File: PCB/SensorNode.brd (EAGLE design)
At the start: 100 x 80 mm, 54 parts, among them Q1 CMA-4544PF-W, U1 MAX4466EXK+T, U2 ESP-WROOM-32, U3 Si7021-A20, U4 MCP73831, U5 TSL2561, U7 V_REG_317SMD

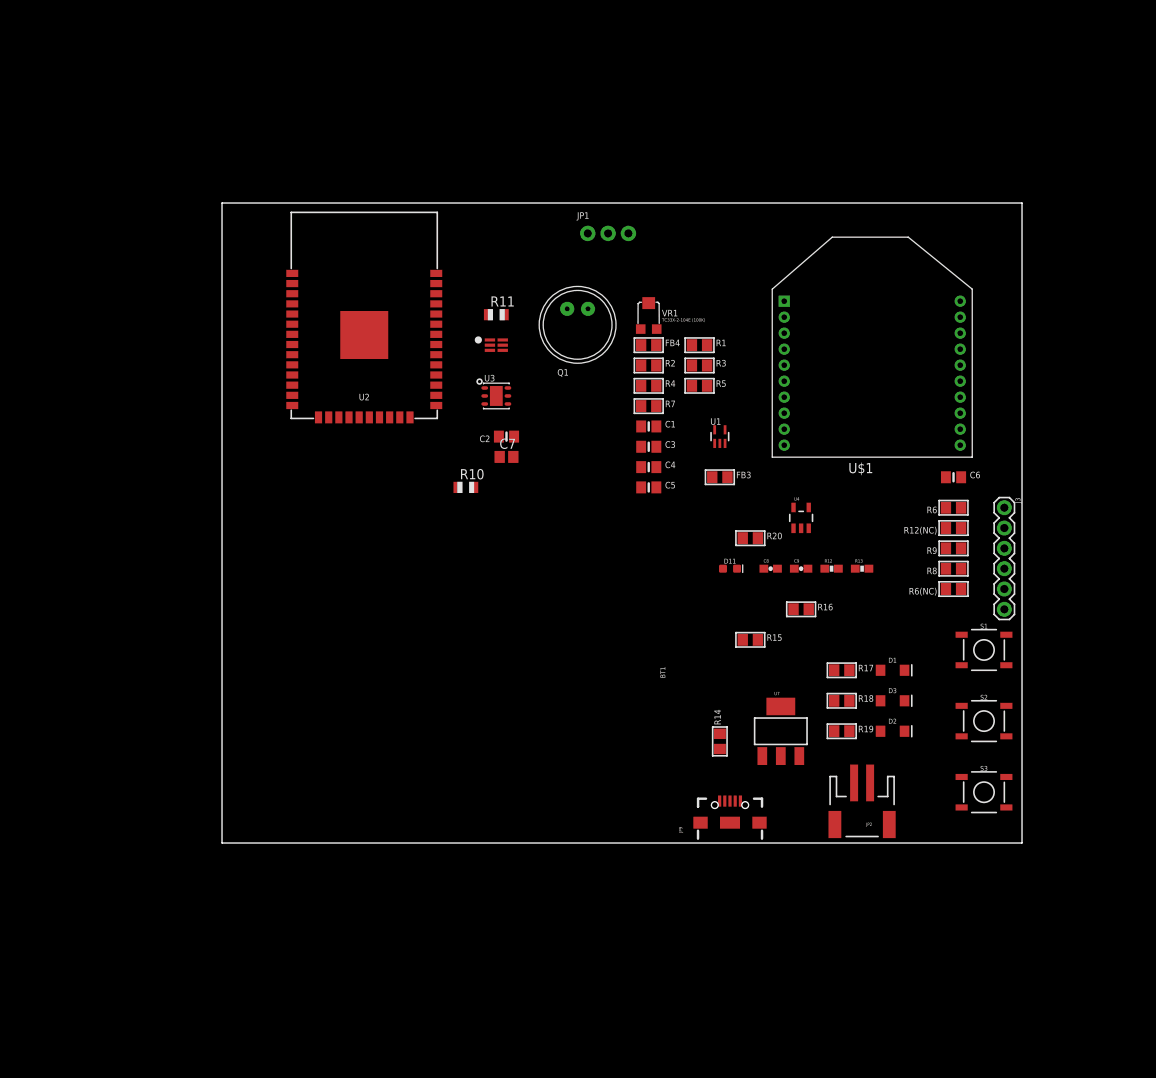
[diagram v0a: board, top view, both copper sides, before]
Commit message: PCB Improvements, layout planned out
Moved components around on layout to minimize pcb space. Battery moved
to back of board. Minor schematic improvements. ESP32 template added
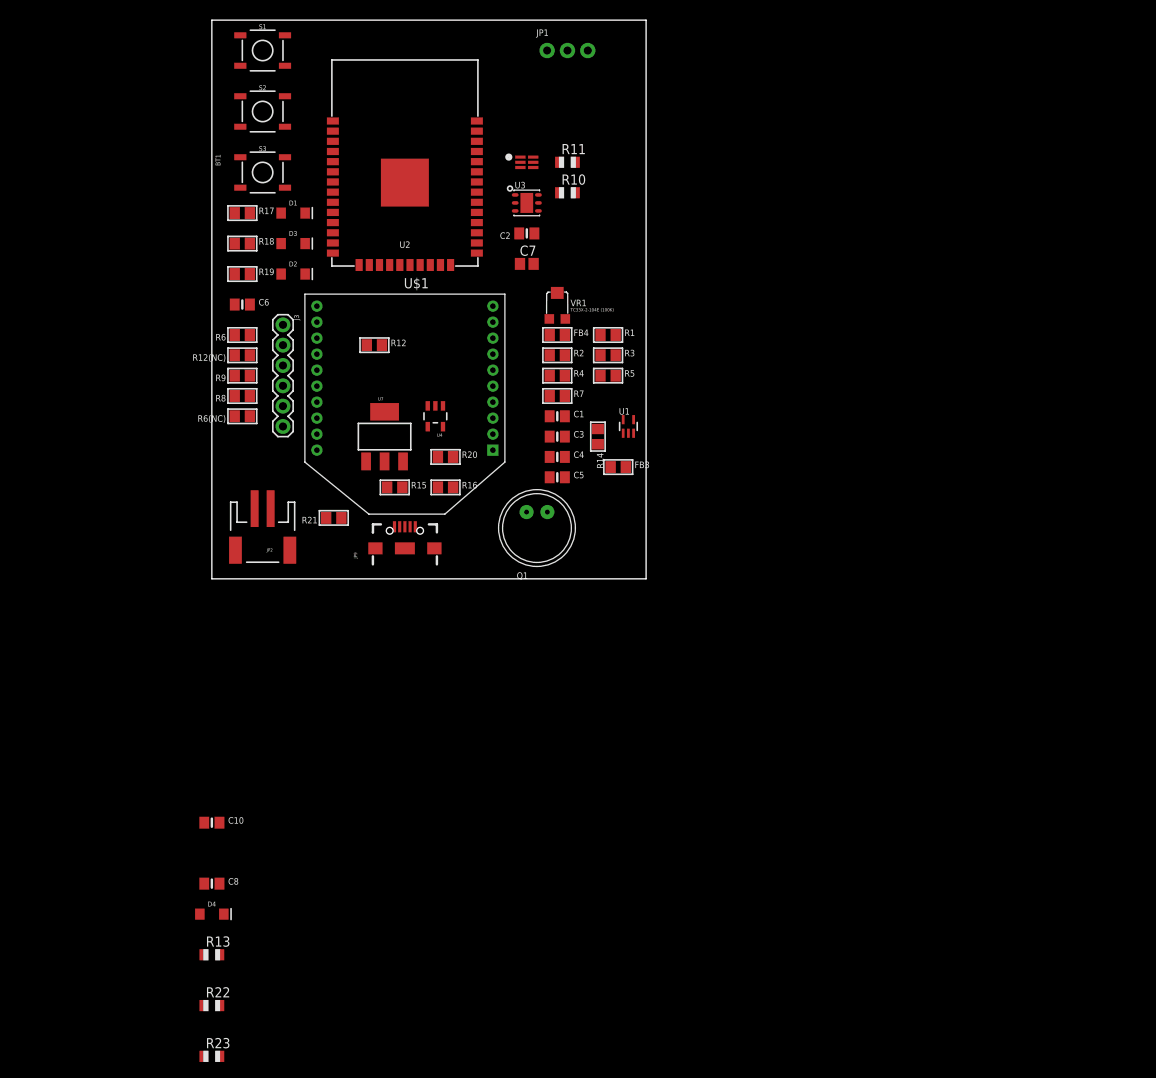
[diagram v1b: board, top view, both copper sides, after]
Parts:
- removed C9: 4.7uF, SparkFun-Capacitors:0603-CAP
- removed D11: RED, SparkFun-LED:LED-0603
- added C10: 4.7uF, microbuilder:0805-NO
- added D4: RED, SparkFun-LED:LED-1206
- added R21: 330, microbuilder:0805
- added R22, R23: 10K, adafruit:R0805
- C8: device SparkFun-Capacitors:0603-CAP -> microbuilder:0805-NO
- R12: value 330 -> 2k; device SparkFun-Resistors:0603-RES -> microbuilder:0805
- R13: value 2.0k -> 10K; device SparkFun-Resistors:0603-RES -> adafruit:R0805
- moved S3 118.9 mm to (5.08, 83.8)
- moved S2 118.1 mm to (5.08, 91.4)
- moved S1 117.2 mm to (5.08, 99.1)
- moved R13 94.5 mm to (-1.27, -14.0)
- moved D2 94.2 mm to (8.89, 71.1)
- moved D3 94.2 mm to (8.89, 74.9)
- moved R18 94.2 mm to (2.54, 74.9)
- moved R19 94.2 mm to (2.54, 71.1)
- moved D1 94.2 mm to (8.89, 78.7)
- moved R17 94.2 mm to (2.54, 78.7)
- moved J3 93.0 mm to (7.62, 64.8)
- moved C6 91.5 mm to (2.54, 67.3)
- moved R12(NC) 91.5 mm to (2.54, 61.0)
- moved R6 91.5 mm to (2.54, 63.5)
- moved R6(NC) 91.5 mm to (2.54, 53.3)
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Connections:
- new net IO23: U2.11
- new net IO25: U2.10
- new net IO33: U2.9
- new net N$35: R13.1, S1.1
- net GND: now also C10.1, C8.1, R12.1; no longer C8.2, C9.2, R13.2
- net N$23: now also D4.A, R21.2; no longer D11.A, R12.1
- net PROG: now also R12.2; no longer R13.1
- net STAT: now also D4.C; no longer D11.C
- net VCC: now also R13.2, R22.2, R23.2; no longer S1.1, S2.1, S3.1
- net VCC_3.7V: now also C8.2; no longer C9.1
- net VIN: now also C10.2, R21.1; no longer C8.1, R12.2
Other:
- board size 100 x 80 mm -> 54.3 x 69.8 mm

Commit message: Added USB to UART and Auto Reset Circuit
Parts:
- removed C7: 0.1uF, adafruit:C0805
- removed J3: (no value), SparkFun-Connectors:1X06
- removed R12(NC), R6(NC): 0K, microbuilder:0805
- added C11: 0.1uF, microbuilder:0805-NO
- added C9: 4.7uF, microbuilder:0805-NO
- added D5: RED, SparkFun-LED:LED-1206
- added D6: GREEN, SparkFun-LED:LED-1206
- added Q2, Q3: 600mA/40V, SparkFun-DiscreteSemi:SOT23-3
- added R24, R25: ???, microbuilder:0805
- added R26: 10K, adafruit:R0805
- added U6: CP2104, microbuilder:QFN24_4MM_SMSC
- R8: value 0K -> 4.7K
- R9: value 0K -> 10K; device microbuilder:0805 -> adafruit:R0805
- moved R13 113.7 mm to (11.4, 99.1), turned to 90 degrees
- moved R22 112.5 mm to (11.4, 91.4), turned to 90 degrees
- moved R23 111.2 mm to (11.4, 83.8), turned to 90 degrees
- moved C8 52.6 mm to (6.35, 47.0), turned to 180 degrees
- moved D4 47.0 mm to (14.0, 35.6)
- moved R9 42.1 mm to (-1.27, 16.5), turned to 0 degrees
- moved C10 38.7 mm to (14.0, 38.1)
- moved JP1 19.1 mm to (24.1, 100.3)
- moved JP2 16.6 mm to (3.81, 54.6)
- moved R8 16.3 mm to (15.2, 45.7), turned to 270 degrees
- moved Q1 7.62 mm to (47.0, 39.4)
- moved U2 1.27 mm to (24.1, 82.5)
- moved JP9 1.27 mm to (22.9, 35.6)
- moved VR1 1.27 mm to (41.9, 68.6), turned to 180 degrees
- turned S1 to 180 degrees
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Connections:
- removed net CTS0: R6(NC).2
- removed net FTDI_CTS: J3.5, R6(NC).1
- removed net FTDI_RTS: J3.1, R12(NC).1
- removed net FTDI_RXD: J3.2, R9.1
- removed net FTDI_TXD: J3.3, R8.1
- removed net FTDI_VCC: J3.4
- removed net RTS0: R12(NC).2
- new net DTR: U6.23
- new net IO0: U2.25
- new net N$36: JP9.D-1, U6.4
- new net N$37: JP9.D+1, U6.3
- new net N$39: U6.21
- new net N$40: U6.20
- new net N$41: D5.A, R24.2
- new net N$42: R24.1, U6.14
- new net N$43: R25.1, U6.13
- new net N$44: D6.A, R25.2
- new net N$46: Q3.3
- new net N$47: Q2.3
- new net N$48: R9.1
- new net N$49: R26.1
- new net RTS: U6.19
- new net TP: U6.THERM
- net GND: now also C11.2, C9.1, D5.C, D6.C, U6.2; no longer C7.2, J3.6
- net N$10: now also C9.2, U6.16; no longer U2.35
- net N$11: now also R8.2, U6.9; no longer U2.34
- net N$13: now also Q2.2, Q3.1, R9.2; no longer U2.36
- net N$14: now also Q2.1, Q3.2, R26.2; no longer U2.31
- net N$35: now also R22.1, R23.1, S2.1, S3.1
- net RXD0: now also U2.34; no longer R8.2
- net TXD0: now also U2.35; no longer R9.2
- net VCC: now also R8.1, U6.5, U6.6
- net VCC_3.7V: now also C11.1; no longer C7.1
- net VIN: now also U6.7, U6.8

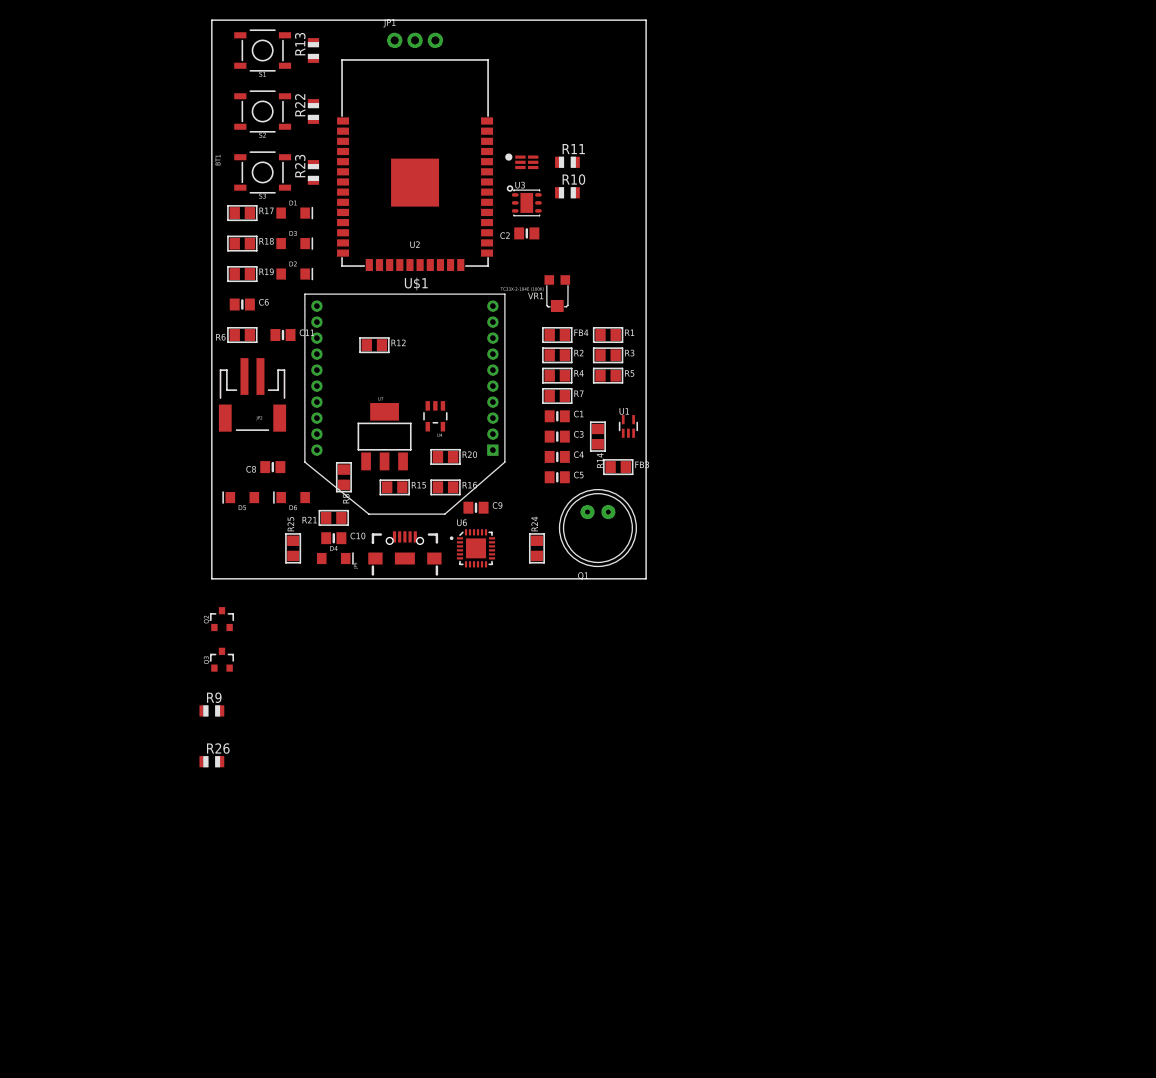
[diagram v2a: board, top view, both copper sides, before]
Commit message: Reset and Bootloader PushButtons, Replaced USB
USB micro to mini due to supply issues.
SMD Xbee headers
New voltage regulator
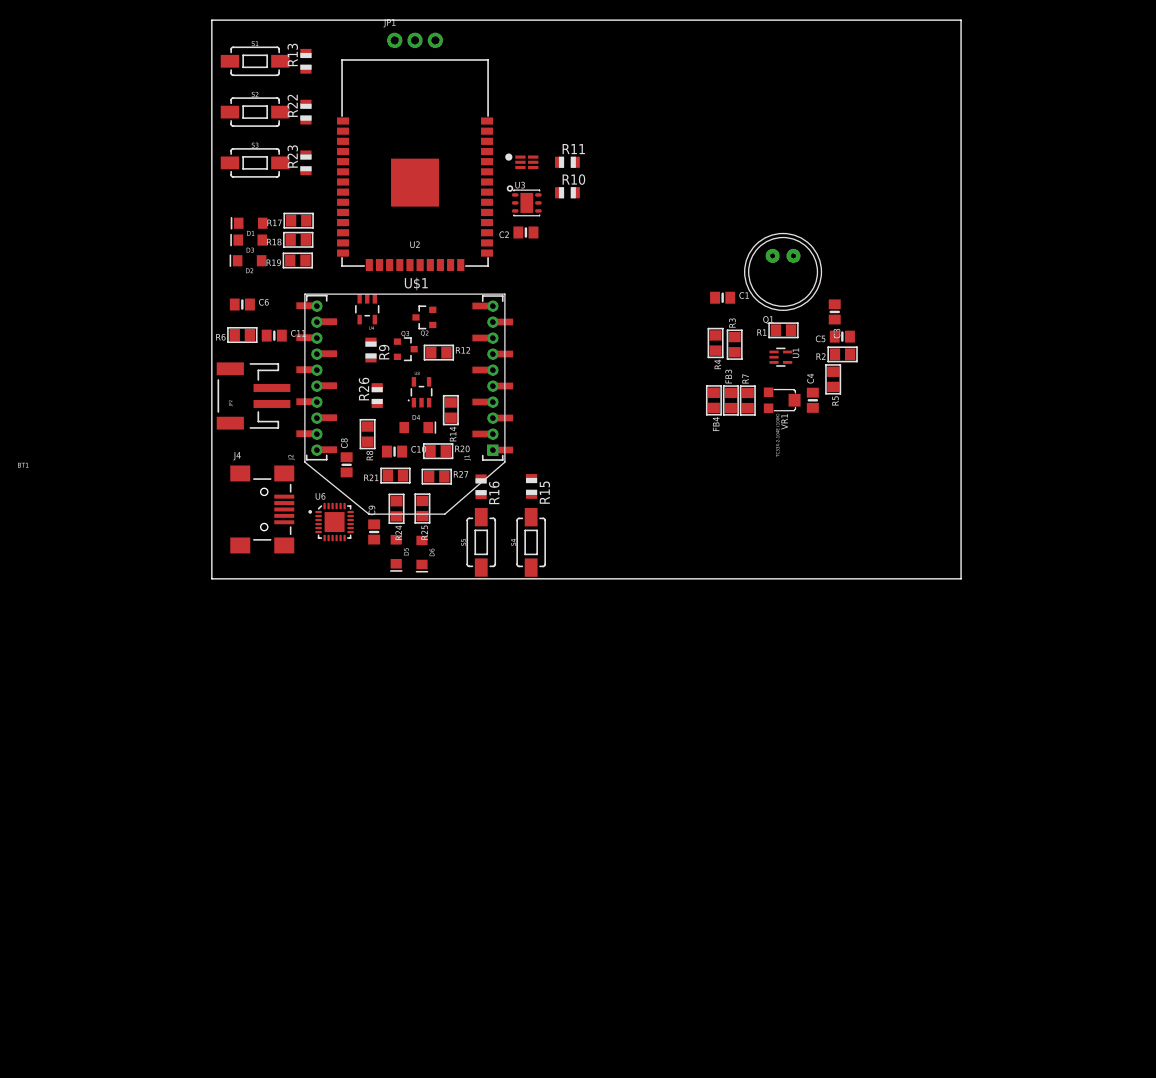
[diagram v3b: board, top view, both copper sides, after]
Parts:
- removed JP9: Micro USB, SparkFun-Connectors:USB-AB-MICRO-SMD_V03
- removed U7: V_REG_317SMD, SparkFun-IC-Power:SOT223
- added J1, J2: (no value), SparkFun-Connectors:1X10-2MM-SMD
- added J4: USB_MINI-B_SMT, SparkFun-Connectors:USB-MINIB
- added R27: 165, microbuilder:0805
- added S4, S5: MOMENTARY-SWITCH-SPST-SMD-6.0X3.5MM, SparkFun-Switches:TACTILE_SWITCH_SMD_6.0X3.5MM
- added U8: 3.3V, SparkFun-IC-Power:SOT23-5
- R14: value ??? -> 2k
- R15: value 370 -> 10K; device microbuilder:0805 -> adafruit:R0805
- R16: value 220 -> 10K; device microbuilder:0805 -> adafruit:R0805
- R20: value ??? -> 20
- R6: value 0K -> 10K
- S1, S2, S3: value MOMENTARY-SWITCH-SPST-SMD-5.2MM -> MOMENTARY-SWITCH-SPST-SMD-6.0X3.5MM; device SparkFun-Switches:TACTILE_SWITCH_SMD_5.2MM -> SparkFun-Switches:TACTILE_SWITCH_SMD_6.0X3.5MM
- moved BT1 66.0 mm to (-8.07, 98.5), turned to 180 degrees
- moved R26 50.2 mm to (19.4, 55.9), turned to 90 degrees
- moved R9 49.3 mm to (18.6, 61.6), turned to 270 degrees
- moved Q2 45.5 mm to (25.3, 65.7), turned to 90 degrees
- moved Q3 45.1 mm to (22.9, 61.7), turned to 270 degrees
- moved C5 39.7 mm to (77.5, 63.3), turned to 180 degrees
- moved Q1 39.5 mm to (70.1, 71.4)
- moved C3 38.0 mm to (76.6, 66.4), turned to 270 degrees
- moved R2 35.7 mm to (77.6, 61.1), turned to 180 degrees
- moved C4 32.7 mm to (73.9, 55.3), turned to 90 degrees
- moved VR1 31.2 mm to (70.1, 55.3), turned to 270 degrees
- moved R5 28.1 mm to (76.4, 58.0), turned to 270 degrees
- moved C1 25.4 mm to (62.6, 68.2)
- moved R7 23.8 mm to (65.7, 55.3), turned to 90 degrees
- moved R1 21.9 mm to (70.2, 64.1), turned to 180 degrees
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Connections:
- net IO23 renamed IO26
- removed net +3V3: C2.1, U3.5
- new net N$38: R16.2, S5.2
- net CTS1: now also J1.9
- net GND: now also J2.10, J4.GND, R27.2, S4.1, S5.1, U8.2; no longer JP9.GND1, R15.1
- net IO7: now also J2.5
- net IO8: now also J2.9
- net N$24: now also S4.2; no longer R16.2, U7.1
- net N$31: now also S1.2; no longer S1.3
- net N$32: now also S2.2; no longer S2.3
- net N$33: now also S3.2; no longer S3.3
- net N$34: now also R27.1
- net N$36: now also J4.D-; no longer JP9.D-1
- net N$37: now also J4.D+; no longer JP9.D+1
- net RTS1: now also J1.5
- net RXD1: now also J2.2
- net TXD1: now also J2.3
- net VCC: now also C2.1, R15.1, U3.5, U8.5; no longer U7.2
- net VCC_3.7V: now also J2.1, U8.1, U8.3; no longer U7.3
- net VIN: now also J4.VBUS; no longer JP9.VBUS1
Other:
- board size 54.3 x 69.8 mm -> 93.6 x 69.8 mm
